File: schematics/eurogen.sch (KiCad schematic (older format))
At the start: 109 parts, among them J1 PJ301M-12, J10 PJ301M-12, J11 PJ301M-12, J12 PJ301M-12, J13 PJ301M-12, J14 PJ301M-12, J2 EURO_PWR_2x5, J3 PJ301M-12, J4 AudioJack3, J5 PJ301M-12, J6 PJ301M-12, J7 PJ301M-12, J8 PJ301M-12, J9 PJ301M-12, SW1 Rotary_Encoder, SW2 SW_Push, SW3 SW_Push, U1 ESP32-DEVKITC-32D, U10 LM1117-3.3, U2 CODECODER-WM8731SEDS_V(SSOP28), U3 MCP3208, U4 CODECODER-WM8731SEDS_V(SSOP28), U5 TL074, U6 LM4040LP-10, U7 MCP6004, U8 MCP6004, U9 LM1117-3.3, Y1 12.288Mhz, Y2 12.288Mhz

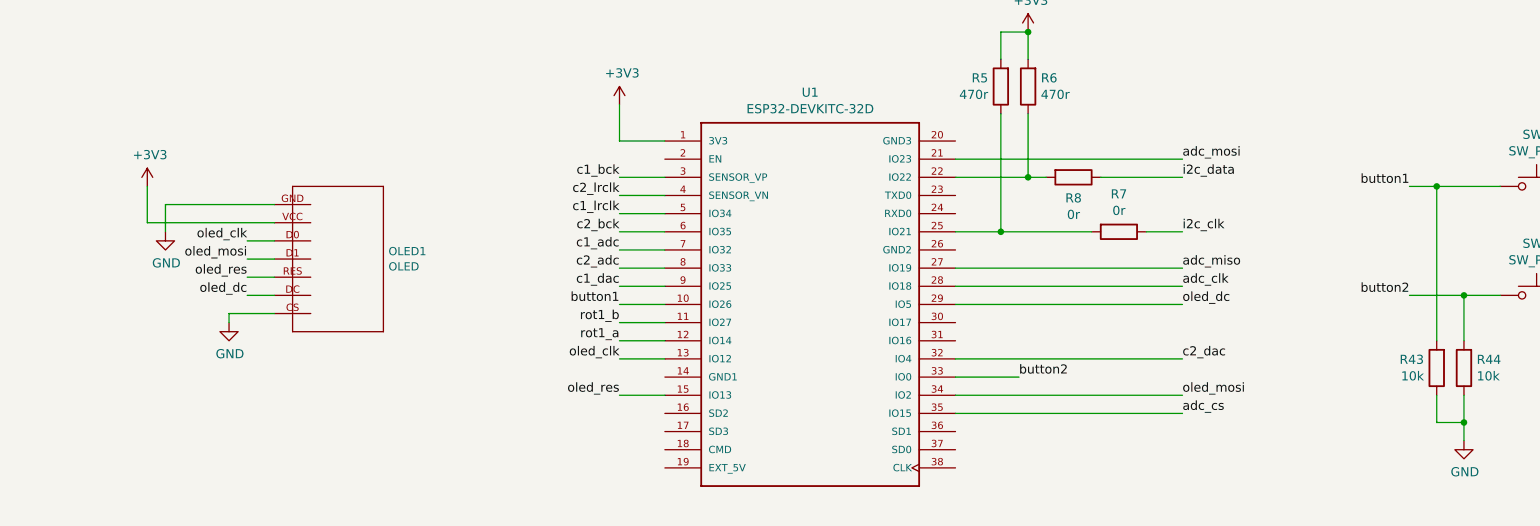
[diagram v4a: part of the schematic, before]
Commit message: pwm led 0, 2 and 5 working
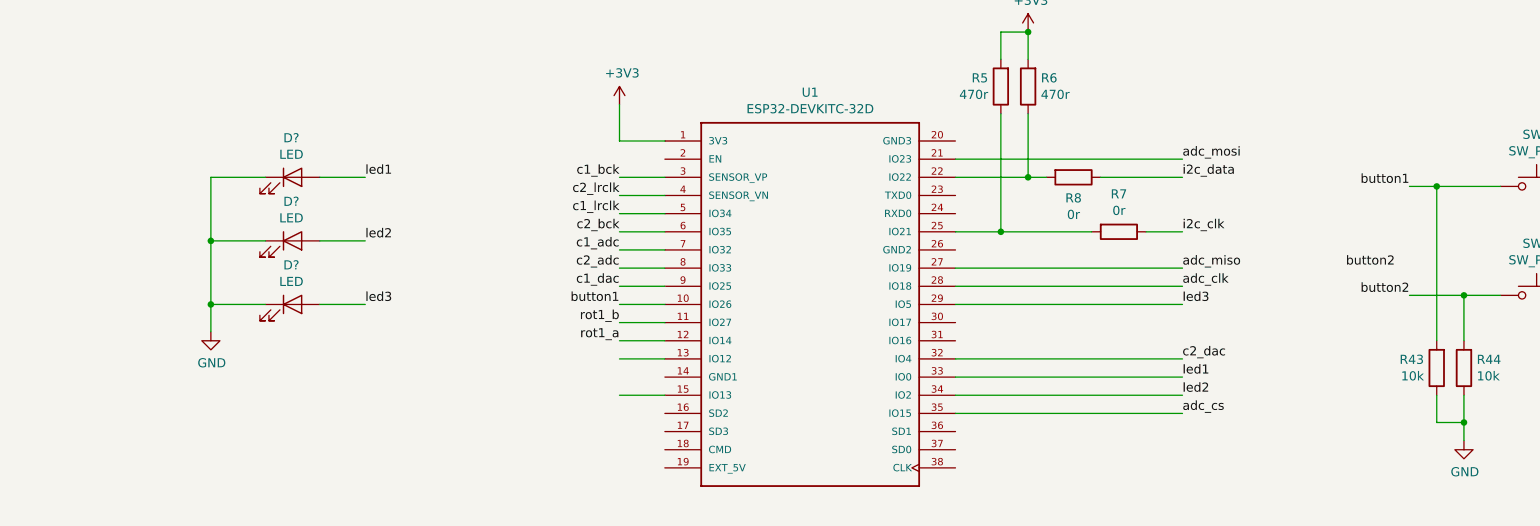
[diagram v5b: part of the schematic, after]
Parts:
- removed OLED1: OLED, oled_OLED_STANDARD, symbol oled:OLED
- added D? (x3): LED, symbol Device:LED
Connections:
- net GND: now also D?.1 (K), D?.1 (K), D?.1 (K)
- net button2: no longer U1.33 (IO0)
- net oled_clk: no longer names the net of U1.13 (IO12)
- net oled_dc renamed led3
- net led3: now also D?.2 (A)
- net oled_mosi renamed led2
- net led2: now also D?.2 (A)
- net oled_res: no longer names the net of U1.15 (IO13)
- new net led1: D?.2 (A), U1.33 (IO0)
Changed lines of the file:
@@
 Wire Wire Line
 	10800 2150 9550 2150
-$Comp
-L oled:OLED OLED1
-U 1 1 5E5B24AA
-P 5900 2000
-F 0 "OLED1" V 5858 2528 45  0000 L CNN
-F 1 "OLED" V 5942 2528 45  0000 L CNN
-F 2 "oled_OLED_STANDARD" H 5930 2150 20  0001 C CNN
-F 3 "" H 5900 2000 50  0001 C CNN
-	1    5900 2000
-	0    1    1    0
-$EndComp
-$Comp
-L power:+3V3 #PWR018
-U 1 1 5E5B7FC9
-P 5100 1600
-F 0 "#PWR018" H 5100 1450 50  0001 C CNN
-F 1 "+3V3" H 5115 1773 50  0000 C CNN
-F 2 "" H 5100 1600 50  0001 C CNN
-F 3 "" H 5100 1600 50  0001 C CNN
-	1    5100 1600
-	1    0    0    -1
-$EndComp
-Wire Wire Line
-	5100 1800 5100 1600
-$Comp
-L power:GND #PWR019
-U 1 1 5E5BBFD5
-P 5200 1850
-F 0 "#PWR019" H 5200 1600 50  0001 C CNN
-F 1 "GND" H 5205 1677 50  0000 C CNN
-F 2 "" H 5200 1850 50  0001 C CNN
-F 3 "" H 5200 1850 50  0001 C CNN
-	1    5200 1850
-	1    0    0    -1
-$EndComp
-Wire Wire Line
-	5200 1850 5200 1700
-Wire Wire Line
-	5200 1700 5800 1700
-Wire Wire Line
-	5100 1800 5800 1800
-Text Label 5650 1900 2    50   ~ 0
-oled_clk
-Text Label 5650 2000 2    50   ~ 0
-oled_mosi
-Text Label 5650 2100 2    50   ~ 0
-oled_res
-Text Label 5650 2200 2    50   ~ 0
-oled_dc
-Wire Wire Line
-	5650 1900 5800 1900
-Wire Wire Line
-	5650 2000 5800 2000
-Wire Wire Line
-	5650 2100 5800 2100
-Wire Wire Line
-	5650 2200 5800 2200
 Wire Wire Line
 	7700 2550 7950 2550
@@
 Text Label 10800 2850 0    50   ~ 0
 adc_cs
-$Comp
-L power:GND #PWR024
-U 1 1 5E6F5531
-P 5550 2350
-F 0 "#PWR024" H 5550 2100 50  0001 C CNN
-F 1 "GND" H 5555 2177 50  0000 C CNN
-F 2 "" H 5550 2350 50  0001 C CNN
-F 3 "" H 5550 2350 50  0001 C CNN
-	1    5550 2350
-	1    0    0    -1
-$EndComp
-Wire Wire Line
-	5550 2350 5550 2300
-Wire Wire Line
-	5550 2300 5800 2300
 Wire Wire Line
 	7700 2450 7950 2450
 Wire Wire Line
 	9550 2850 10800 2850
-Text Label 7700 2550 2    50   ~ 0
-oled_clk
-Text Label 10800 2750 0    50   ~ 0
-oled_mosi
 Wire Wire Line
 	9550 2750 10800 2750
-Text Label 7700 2750 2    50   ~ 0
-oled_res
-Text Label 10800 2250 0    50   ~ 0
-oled_dc
 Wire Wire Line
 	9550 2250 10800 2250
@@
 Text Label 7700 2250 2    50   ~ 0
 button1
-Text Label 9900 2650 0    50   ~ 0
+Text Label 11700 2050 0    50   ~ 0
 button2
-Wire Wire Line
-	9900 2650 9550 2650
 Text Label 12050 1600 2    50   ~ 0
 button1
@@
 Text Label 13150 5300 0    50   ~ 0
 audio_in4
+$Comp
+L Device:LED D?
+U 1 1 5E97629B
+P 5900 1550
+F 0 "D?" H 5893 1766 50  0000 C CNN
+F 1 "LED" H 5893 1675 50  0000 C CNN
+F 2 "" H 5900 1550 50  0001 C CNN
+F 3 "~" H 5900 1550 50  0001 C CNN
+	1    5900 1550
+	1    0    0    -1
+$EndComp
+$Comp
+L Device:LED D?
+U 1 1 5E97741F
+P 5900 1900
+F 0 "D?" H 5893 2116 50  0000 C CNN
+F 1 "LED" H 5893 2025 50  0000 C CNN
+F 2 "" H 5900 1900 50  0001 C CNN
+F 3 "~" H 5900 1900 50  0001 C CNN
+	1    5900 1900
+	1    0    0    -1
+$EndComp
+$Comp
+L Device:LED D?
+U 1 1 5E978540
+P 5900 2250
+F 0 "D?" H 5893 2466 50  0000 C CNN
+F 1 "LED" H 5893 2375 50  0000 C CNN
+F 2 "" H 5900 2250 50  0001 C CNN
+F 3 "~" H 5900 2250 50  0001 C CNN
+	1    5900 2250
+	1    0    0    -1
+$EndComp
+$Comp
+L power:GND #PWR?
+U 1 1 5E978B47
+P 5450 2400
+F 0 "#PWR?" H 5450 2150 50  0001 C CNN
+F 1 "GND" H 5455 2227 50  0000 C CNN
+F 2 "" H 5450 2400 50  0001 C CNN
+F 3 "" H 5450 2400 50  0001 C CNN
+	1    5450 2400
+	1    0    0    -1
+$EndComp
+Wire Wire Line
+	5750 1550 5450 1550
+Wire Wire Line
+	5450 1550 5450 1900
+Wire Wire Line
+	5750 1900 5450 1900
+Connection ~ 5450 1900
+Wire Wire Line
+	5450 1900 5450 2250
+Wire Wire Line
+	5750 2250 5450 2250
+Connection ~ 5450 2250
+Wire Wire Line
+	5450 2250 5450 2400
+Text Label 6300 1550 0    50   ~ 0
+led1
+Text Label 6300 1900 0    50   ~ 0
+led2
+Text Label 6300 2250 0    50   ~ 0
+led3
+Wire Wire Line
+	6050 1550 6300 1550
+Wire Wire Line
+	6050 1900 6300 1900
+Wire Wire Line
+	6050 2250 6300 2250
+Text Label 10800 2650 0    50   ~ 0
+led1
+Wire Wire Line
+	9550 2650 10800 2650
+Text Label 10800 2750 0    50   ~ 0
+led2
+Text Label 10800 2250 0    50   ~ 0
+led3
 $EndSCHEMATC

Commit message: sendhook implemented
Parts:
- removed SW1: Rotary_Encoder, symbol Device:Rotary_Encoder
- added R49, R50, R51: 220r, symbol Device:R
- gave numbers to parts that had none: 3
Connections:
- net button2: now also U1.13 (IO12)
- net led1: now also R49.2; no longer D1.2 (A)
- net led2: now also R50.2; no longer D2.2 (A)
- net led3: now also R51.2; no longer D3.2 (A)
- net rot1_a: no longer names the net of U1.12 (IO14)
- net rot1_b: no longer names the net of U1.11 (IO27)
- new net: D1.2 (A), R49.1
- new net: D2.2 (A), R50.1
- new net: D3.2 (A), R51.1
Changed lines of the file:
@@
 Wire Wire Line
 	7700 2750 7950 2750
-$Comp
-L Device:Rotary_Encoder SW1
-U 1 1 5E5B9F74
-P 15450 1600
-F 0 "SW1" H 15680 1646 50  0000 L CNN
-F 1 "Rotary_Encoder" H 15680 1555 50  0000 L CNN
-F 2 "" H 15300 1760 50  0001 C CNN
-F 3 "~" H 15450 1860 50  0001 C CNN
-	1    15450 1600
-	1    0    0    -1
-$EndComp
-$Comp
-L power:GND #PWR022
-U 1 1 5E5BCC80
-P 14350 1700
-F 0 "#PWR022" H 14350 1450 50  0001 C CNN
-F 1 "GND" H 14355 1527 50  0000 C CNN
-F 2 "" H 14350 1700 50  0001 C CNN
-F 3 "" H 14350 1700 50  0001 C CNN
-	1    14350 1700
-	1    0    0    -1
-$EndComp
-Wire Wire Line
-	15150 1600 14350 1600
-Wire Wire Line
-	14350 1600 14350 1700
-Text Label 14900 1500 2    50   ~ 0
-rot1_a
-Text Label 14900 1700 2    50   ~ 0
-rot1_b
-Wire Wire Line
-	14900 1700 15150 1700
-Wire Wire Line
-	15150 1500 14900 1500
 Wire Wire Line
 	7700 1950 7950 1950
@@
 Wire Wire Line
 	9550 2250 10800 2250
-Text Label 7700 2450 2    50   ~ 0
-rot1_a
-Text Label 7700 2350 2    50   ~ 0
-rot1_b
 $Comp
 L CODECODER-WM8731SEDS_V_SSOP28_:CODECODER-WM8731SEDS_V(SSOP28) U4
@@
 Text Label 7700 2250 2    50   ~ 0
 button1
-Text Label 11700 2050 0    50   ~ 0
+Text Label 7700 2550 2    50   ~ 0
 button2
 Text Label 12050 1600 2    50   ~ 0
@@
 audio_in4
 $Comp
-L Device:LED D?
+L Device:LED D1
 U 1 1 5E97629B
 P 5900 1550
-F 0 "D?" H 5893 1766 50  0000 C CNN
+F 0 "D1" H 5893 1766 50  0000 C CNN
 F 1 "LED" H 5893 1675 50  0000 C CNN
 F 2 "" H 5900 1550 50  0001 C CNN
@@
 $EndComp
 $Comp
-L Device:LED D?
+L Device:LED D2
 U 1 1 5E97741F
 P 5900 1900
-F 0 "D?" H 5893 2116 50  0000 C CNN
+F 0 "D2" H 5893 2116 50  0000 C CNN
 F 1 "LED" H 5893 2025 50  0000 C CNN
 F 2 "" H 5900 1900 50  0001 C CNN
@@
 $EndComp
 $Comp
-L Device:LED D?
+L Device:LED D3
 U 1 1 5E978540
 P 5900 2250
-F 0 "D?" H 5893 2466 50  0000 C CNN
+F 0 "D3" H 5893 2466 50  0000 C CNN
 F 1 "LED" H 5893 2375 50  0000 C CNN
 F 2 "" H 5900 2250 50  0001 C CNN
@@
 $EndComp
 $Comp
-L power:GND #PWR?
+L power:GND #PWR018
 U 1 1 5E978B47
 P 5450 2400
-F 0 "#PWR?" H 5450 2150 50  0001 C CNN
+F 0 "#PWR018" H 5450 2150 50  0001 C CNN
 F 1 "GND" H 5455 2227 50  0000 C CNN
 F 2 "" H 5450 2400 50  0001 C CNN
@@
 Wire Wire Line
 	5450 2250 5450 2400
-Text Label 6300 1550 0    50   ~ 0
+Text Label 6650 1550 0    50   ~ 0
 led1
-Text Label 6300 1900 0    50   ~ 0
+Text Label 6650 1900 0    50   ~ 0
 led2
-Text Label 6300 2250 0    50   ~ 0
+Text Label 6650 2250 0    50   ~ 0
 led3
-Wire Wire Line
-	6050 1550 6300 1550
-Wire Wire Line
-	6050 1900 6300 1900
-Wire Wire Line
-	6050 2250 6300 2250
 Text Label 10800 2650 0    50   ~ 0
 led1
@@
 Text Label 10800 2250 0    50   ~ 0
 led3
+$Comp
+L Device:R R49
+U 1 1 5EAFC261
+P 6350 1550
+F 0 "R49" V 6557 1550 50  0000 C CNN
+F 1 "220r" V 6466 1550 50  0000 C CNN
+F 2 "" V 6280 1550 50  0001 C CNN
+F 3 "~" H 6350 1550 50  0001 C CNN
+	1    6350 1550
+	0    -1   -1   0
+$EndComp
+$Comp
+L Device:R R50
+U 1 1 5EAFD1AE
+P 6350 1900
+F 0 "R50" V 6557 1900 50  0000 C CNN
+F 1 "220r" V 6466 1900 50  0000 C CNN
+F 2 "" V 6280 1900 50  0001 C CNN
+F 3 "~" H 6350 1900 50  0001 C CNN
+	1    6350 1900
+	0    -1   -1   0
+$EndComp
+$Comp
+L Device:R R51
+U 1 1 5EAFD53B
+P 6350 2250
+F 0 "R51" V 6557 2250 50  0000 C CNN
+F 1 "220r" V 6466 2250 50  0000 C CNN
+F 2 "" V 6280 2250 50  0001 C CNN
+F 3 "~" H 6350 2250 50  0001 C CNN
+	1    6350 2250
+	0    -1   -1   0
+$EndComp
+Wire Wire Line
+	6050 1550 6200 1550
+Wire Wire Line
+	6050 1900 6200 1900
+Wire Wire Line
+	6050 2250 6200 2250
+Wire Wire Line
+	6500 1550 6650 1550
+Wire Wire Line
+	6500 1900 6650 1900
+Wire Wire Line
+	6500 2250 6650 2250
 $EndSCHEMATC

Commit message: led fixes and small cleanup
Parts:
- added D?: LED, symbol Device:LED
- added R?: 220r, symbol Device:R
- added R?: 10k, symbol Device:R
- added SW?: SW_Push, symbol Switch:SW_Push
- R22: value 27k -> 28k
- R26: value 27k -> 25k7
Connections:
- net +3V3: now also SW?.2
- net GND: now also D?.1 (K), R?.1
- net button3: now reaches U1.11 (IO27)
- net button3: now also R?.2, SW?.1
- net led4: now reaches U1.12 (IO14)
- net led4: now also R?.2
- new net: D?.2 (A), R?.1
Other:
- moved on the sheet: R43, R44, SW3
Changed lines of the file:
@@
 P 8150 7650
 F 0 "R26" V 8357 7650 50  0000 C CNN
-F 1 "27k" V 8266 7650 50  0000 C CNN
+F 1 "25k7" V 8266 7650 50  0000 C CNN
 F 2 "" V 8080 7650 50  0001 C CNN
 F 3 "~" H 8150 7650 50  0001 C CNN
@@
 P 7400 7400
 F 0 "R22" V 7607 7400 50  0000 C CNN
-F 1 "27k" V 7516 7400 50  0000 C CNN
+F 1 "28k" V 7516 7400 50  0000 C CNN
 F 2 "" V 7330 7400 50  0001 C CNN
 F 3 "~" H 7400 7400 50  0001 C CNN
@@
 L Switch:SW_Push SW3
 U 1 1 5F9165B3
-P 12750 2200
-F 0 "SW3" H 12750 2485 50  0000 C CNN
-F 1 "SW_Push" H 12750 2394 50  0000 C CNN
-F 2 "" H 12750 2400 50  0001 C CNN
-F 3 "~" H 12750 2400 50  0001 C CNN
-	1    12750 2200
+P 12750 2000
+F 0 "SW3" H 12750 2285 50  0000 C CNN
+F 1 "SW_Push" H 12750 2194 50  0000 C CNN
+F 2 "" H 12750 2200 50  0001 C CNN
+F 3 "~" H 12750 2200 50  0001 C CNN
+	1    12750 2000
 	1    0    0    -1
 $EndComp
@@
 Wire Wire Line
 	13250 1600 12950 1600
-Wire Wire Line
-	12950 2200 13250 2200
-Wire Wire Line
-	13250 2200 13250 1600
-Connection ~ 13250 1600
 Text Label 7700 2250 2    50   ~ 0
 button1
@@
 Text Label 12050 1600 2    50   ~ 0
 button1
-Text Label 12050 2200 2    50   ~ 0
+Text Label 12050 2000 2    50   ~ 0
 button2
 $Comp
 L Device:R R43
 U 1 1 5F9A139D
-P 12200 2600
-F 0 "R43" H 12270 2554 50  0000 L CNN
-F 1 "10k" H 12270 2645 50  0000 L CNN
-F 2 "" V 12130 2600 50  0001 C CNN
-F 3 "~" H 12200 2600 50  0001 C CNN
-	1    12200 2600
+P 12200 3000
+F 0 "R43" H 12269 2954 50  0000 L CNN
+F 1 "10k" H 12269 3045 50  0000 L CNN
+F 2 "" V 12130 3000 50  0001 C CNN
+F 3 "~" H 12200 3000 50  0001 C CNN
+	1    12200 3000
 	-1   0    0    1
 $EndComp
@@
 L Device:R R44
 U 1 1 5F9A1BAD
-P 12350 2600
-F 0 "R44" H 12280 2554 50  0000 R CNN
-F 1 "10k" H 12280 2645 50  0000 R CNN
-F 2 "" V 12280 2600 50  0001 C CNN
-F 3 "~" H 12350 2600 50  0001 C CNN
-	1    12350 2600
+P 12350 3000
+F 0 "R44" H 12280 2954 50  0000 R CNN
+F 1 "10k" H 12280 3045 50  0000 R CNN
+F 2 "" V 12280 3000 50  0001 C CNN
+F 3 "~" H 12350 3000 50  0001 C CNN
+	1    12350 3000
 	-1   0    0    1
 $EndComp
@@
 L power:GND #PWR082
 U 1 1 5F9A2727
-P 12350 3000
-F 0 "#PWR082" H 12350 2750 50  0001 C CNN
-F 1 "GND" H 12355 2827 50  0000 C CNN
-F 2 "" H 12350 3000 50  0001 C CNN
-F 3 "" H 12350 3000 50  0001 C CNN
-	1    12350 3000
-	1    0    0    -1
-$EndComp
-Wire Wire Line
-	12350 2750 12350 2900
-Wire Wire Line
-	12200 2750 12200 2900
-Wire Wire Line
-	12200 2900 12350 2900
-Connection ~ 12350 2900
-Wire Wire Line
-	12350 2900 12350 3000
-Wire Wire Line
-	12550 2200 12350 2200
-Wire Wire Line
-	12550 1600 12200 1600
-Wire Wire Line
-	12200 2450 12200 1600
-Connection ~ 12200 1600
-Wire Wire Line
-	12200 1600 12050 1600
-Wire Wire Line
-	12350 2450 12350 2200
-Connection ~ 12350 2200
-Wire Wire Line
-	12350 2200 12050 2200
+P 12350 3400
+F 0 "#PWR082" H 12350 3150 50  0001 C CNN
+F 1 "GND" H 12355 3227 50  0000 C CNN
+F 2 "" H 12350 3400 50  0001 C CNN
+F 3 "" H 12350 3400 50  0001 C CNN
+	1    12350 3400
+	1    0    0    -1
+$EndComp
+Wire Wire Line
+	12350 3150 12350 3300
+Wire Wire Line
+	12200 3150 12200 3300
+Wire Wire Line
+	12200 3300 12350 3300
+Connection ~ 12350 3300
+Wire Wire Line
+	12350 3300 12350 3400
 $Comp
 L eurocad:PJ301M-12 J13
@@
 L power:GND #PWR018
 U 1 1 5E978B47
-P 5450 2400
-F 0 "#PWR018" H 5450 2150 50  0001 C CNN
-F 1 "GND" H 5455 2227 50  0000 C CNN
-F 2 "" H 5450 2400 50  0001 C CNN
-F 3 "" H 5450 2400 50  0001 C CNN
-	1    5450 2400
+P 5450 2900
+F 0 "#PWR018" H 5450 2650 50  0001 C CNN
+F 1 "GND" H 5455 2727 50  0000 C CNN
+F 2 "" H 5450 2900 50  0001 C CNN
+F 3 "" H 5450 2900 50  0001 C CNN
+	1    5450 2900
 	1    0    0    -1
 $EndComp
@@
 Wire Wire Line
 	5750 2250 5450 2250
-Connection ~ 5450 2250
-Wire Wire Line
-	5450 2250 5450 2400
 Text Label 6650 1550 0    50   ~ 0
 led1
@@
 Wire Wire Line
 	6500 2250 6650 2250
+$Comp
+L Device:LED D?
+U 1 1 5EA8E0BE
+P 5900 2600
+F 0 "D?" H 5893 2816 50  0000 C CNN
+F 1 "LED" H 5893 2725 50  0000 C CNN
+F 2 "" H 5900 2600 50  0001 C CNN
+F 3 "~" H 5900 2600 50  0001 C CNN
+	1    5900 2600
+	1    0    0    -1
+$EndComp
+Wire Wire Line
+	5750 2600 5450 2600
+$Comp
+L Device:R R?
+U 1 1 5EA8E0C7
+P 6350 2600
+F 0 "R?" V 6557 2600 50  0000 C CNN
+F 1 "220r" V 6466 2600 50  0000 C CNN
+F 2 "" V 6280 2600 50  0001 C CNN
+F 3 "~" H 6350 2600 50  0001 C CNN
+	1    6350 2600
+	0    -1   -1   0
+$EndComp
+Wire Wire Line
+	6050 2600 6200 2600
+Wire Wire Line
+	6500 2600 6650 2600
+Wire Wire Line
+	5450 2250 5450 2600
+Connection ~ 5450 2250
+Wire Wire Line
+	5450 2900 5450 2600
+Connection ~ 5450 2600
+Text Label 6650 2600 0    50   ~ 0
+led4
+Text Label 7700 2450 2    50   ~ 0
+led4
+Wire Wire Line
+	12050 2000 12350 2000
+Wire Wire Line
+	12050 1600 12200 1600
+$Comp
+L Switch:SW_Push SW?
+U 1 1 5EBAF086
+P 12750 2400
+F 0 "SW?" H 12750 2685 50  0000 C CNN
+F 1 "SW_Push" H 12750 2594 50  0000 C CNN
+F 2 "" H 12750 2600 50  0001 C CNN
+F 3 "~" H 12750 2600 50  0001 C CNN
+	1    12750 2400
+	1    0    0    -1
+$EndComp
+Wire Wire Line
+	12950 2400 13250 2400
+Text Label 12050 2400 2    50   ~ 0
+button3
+Wire Wire Line
+	13250 1600 13250 2000
+Wire Wire Line
+	13250 2000 12950 2000
+Connection ~ 13250 1600
+Wire Wire Line
+	13250 2000 13250 2400
+Connection ~ 13250 2000
+$Comp
+L Device:R R?
+U 1 1 5EDE36DC
+P 12650 3000
+F 0 "R?" H 12580 2954 50  0000 R CNN
+F 1 "10k" H 12580 3045 50  0000 R CNN
+F 2 "" V 12580 3000 50  0001 C CNN
+F 3 "~" H 12650 3000 50  0001 C CNN
+	1    12650 3000
+	-1   0    0    1
+$EndComp
+Wire Wire Line
+	12350 2000 12350 2850
+Connection ~ 12350 2000
+Wire Wire Line
+	12350 2000 12550 2000
+Wire Wire Line
+	12200 2850 12200 1600
+Connection ~ 12200 1600
+Wire Wire Line
+	12200 1600 12550 1600
+Wire Wire Line
+	12050 2400 12500 2400
+Wire Wire Line
+	12650 2850 12650 2750
+Wire Wire Line
+	12650 2750 12500 2750
+Wire Wire Line
+	12500 2750 12500 2400
+Connection ~ 12500 2400
+Wire Wire Line
+	12500 2400 12550 2400
+Wire Wire Line
+	12650 3150 12650 3300
+Wire Wire Line
+	12350 3300 12650 3300
+Text Label 7700 2350 2    50   ~ 0
+button3
 $EndSCHEMATC

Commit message: wm8731 fixes
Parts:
- J1, J10, J11, J12, J13, J14, J3, J5, J6, J7, J8, J9: symbol eurocad:PJ301M-12 -> eurogen-rescue:PJ301M-12-eurocad
- J2: symbol eurocad:EURO_PWR_2x5 -> eurogen-rescue:EURO_PWR_2x5-eurocad
- U1: symbol ESP32-DEVKITC-32D:ESP32-DEVKITC-32D -> eurogen-rescue:ESP32-DEVKITC-32D-ESP32-DEVKITC-32D
- U2, U4: symbol CODECODER-WM8731SEDS_V_SSOP28_:CODECODER-WM8731SEDS_V(SSOP28) -> eurogen-rescue:CODECODER-WM8731SEDS_V(SSOP28)-CODECODER-WM8731SEDS_V_SSOP28_
- gave numbers to parts that had none: 4
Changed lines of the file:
@@
 $EndDescr
 $Comp
-L ESP32-DEVKITC-32D:ESP32-DEVKITC-32D U1
+L eurogen-rescue:ESP32-DEVKITC-32D-ESP32-DEVKITC-32D U1
 U 1 1 5E52B8F6
 P 8750 2250
@@
 $EndComp
 $Comp
-L CODECODER-WM8731SEDS_V_SSOP28_:CODECODER-WM8731SEDS_V(SSOP28) U2
+L eurogen-rescue:CODECODER-WM8731SEDS_V(SSOP28)-CODECODER-WM8731SEDS_V_SSOP28_ U2
 U 1 1 5E52D4BC
 P 7100 5000
@@
 $EndComp
 $Comp
-L eurocad:PJ301M-12 J3
+L eurogen-rescue:PJ301M-12-eurocad J3
 U 1 1 5E53783B
 P 1250 1250
@@
 	3650 1100 3900 1100
 $Comp
-L eurocad:PJ301M-12 J1
+L eurogen-rescue:PJ301M-12-eurocad J1
 U 1 1 5E576246
 P 1250 2400
@@
 	9550 2250 10800 2250
 $Comp
-L CODECODER-WM8731SEDS_V_SSOP28_:CODECODER-WM8731SEDS_V(SSOP28) U4
+L eurogen-rescue:CODECODER-WM8731SEDS_V(SSOP28)-CODECODER-WM8731SEDS_V_SSOP28_ U4
 U 1 1 5E790E42
 P 12400 5050
@@
 	2900 8200 3050 8200
 $Comp
-L eurocad:EURO_PWR_2x5 J2
+L eurogen-rescue:EURO_PWR_2x5-eurocad J2
 U 1 1 5E797AD5
 P 20450 1650
@@
 	2200 7350 2450 7350
 $Comp
-L eurocad:PJ301M-12 J5
+L eurogen-rescue:PJ301M-12-eurocad J5
 U 1 1 5E7A9D33
 P 5150 8250
@@
 	2200 8950 2450 8950
 $Comp
-L eurocad:PJ301M-12 J6
+L eurogen-rescue:PJ301M-12-eurocad J6
 U 1 1 5E809BFE
 P 5150 9850
@@
 	7000 7400 7250 7400
 $Comp
-L eurocad:PJ301M-12 J7
+L eurogen-rescue:PJ301M-12-eurocad J7
 U 1 1 5E88AFDE
 P 9950 8300
@@
 	7000 9000 7250 9000
 $Comp
-L eurocad:PJ301M-12 J8
+L eurogen-rescue:PJ301M-12-eurocad J8
 U 1 1 5E88B025
 P 9950 9900
@@
 $EndComp
 $Comp
-L eurocad:PJ301M-12 J9
+L eurogen-rescue:PJ301M-12-eurocad J9
 U 1 1 5ECC9FEC
 P 13600 10900
@@
 CV in -> 0/3V3\n
 $Comp
-L eurocad:PJ301M-12 J10
+L eurogen-rescue:PJ301M-12-eurocad J10
 U 1 1 5EE79B53
 P 13550 12700
@@
 CV in -> 0/3V3\n
 $Comp
-L eurocad:PJ301M-12 J12
+L eurogen-rescue:PJ301M-12-eurocad J12
 U 1 1 5EEA65DB
 P 18150 10900
@@
 CV in -> 0/3V3\n
 $Comp
-L eurocad:PJ301M-12 J11
+L eurogen-rescue:PJ301M-12-eurocad J11
 U 1 1 5EEA6613
 P 18100 12700
@@
 	12350 3300 12350 3400
 $Comp
-L eurocad:PJ301M-12 J13
+L eurogen-rescue:PJ301M-12-eurocad J13
 U 1 1 5FD14493
 P 1250 3600
@@
 	3650 3450 3900 3450
 $Comp
-L eurocad:PJ301M-12 J14
+L eurogen-rescue:PJ301M-12-eurocad J14
 U 1 1 5FD144D1
 P 1250 4750
@@
 	6500 2250 6650 2250
 $Comp
-L Device:LED D?
+L Device:LED D4
 U 1 1 5EA8E0BE
 P 5900 2600
-F 0 "D?" H 5893 2816 50  0000 C CNN
+F 0 "D4" H 5893 2816 50  0000 C CNN
 F 1 "LED" H 5893 2725 50  0000 C CNN
 F 2 "" H 5900 2600 50  0001 C CNN
@@
 	5750 2600 5450 2600
 $Comp
-L Device:R R?
+L Device:R R52
 U 1 1 5EA8E0C7
 P 6350 2600
-F 0 "R?" V 6557 2600 50  0000 C CNN
+F 0 "R52" V 6557 2600 50  0000 C CNN
 F 1 "220r" V 6466 2600 50  0000 C CNN
 F 2 "" V 6280 2600 50  0001 C CNN
@@
 	12050 1600 12200 1600
 $Comp
-L Switch:SW_Push SW?
+L Switch:SW_Push SW1
 U 1 1 5EBAF086
 P 12750 2400
-F 0 "SW?" H 12750 2685 50  0000 C CNN
+F 0 "SW1" H 12750 2685 50  0000 C CNN
 F 1 "SW_Push" H 12750 2594 50  0000 C CNN
 F 2 "" H 12750 2600 50  0001 C CNN
@@
 Connection ~ 13250 2000
 $Comp
-L Device:R R?
+L Device:R R53
 U 1 1 5EDE36DC
 P 12650 3000
-F 0 "R?" H 12580 2954 50  0000 R CNN
+F 0 "R53" H 12580 2954 50  0000 R CNN
 F 1 "10k" H 12580 3045 50  0000 R CNN
 F 2 "" V 12580 3000 50  0001 C CNN
